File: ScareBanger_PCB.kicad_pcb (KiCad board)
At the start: 2 copper layers, 76 x 56 mm, 17 parts, among them J1 RJ45, J16 Conn_01x10_Female - SAINSMART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, J17 Screw_Terminal_01x10 - HILETG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, J2 1757271, J3 Screw_Terminal_01x06, J4 Barrel_Jack_Switch, J6 Screw_Terminal_01x06, J7 Screw_Terminal_01x06, SW1 SW_SPDT, SW2 SW_SPDT

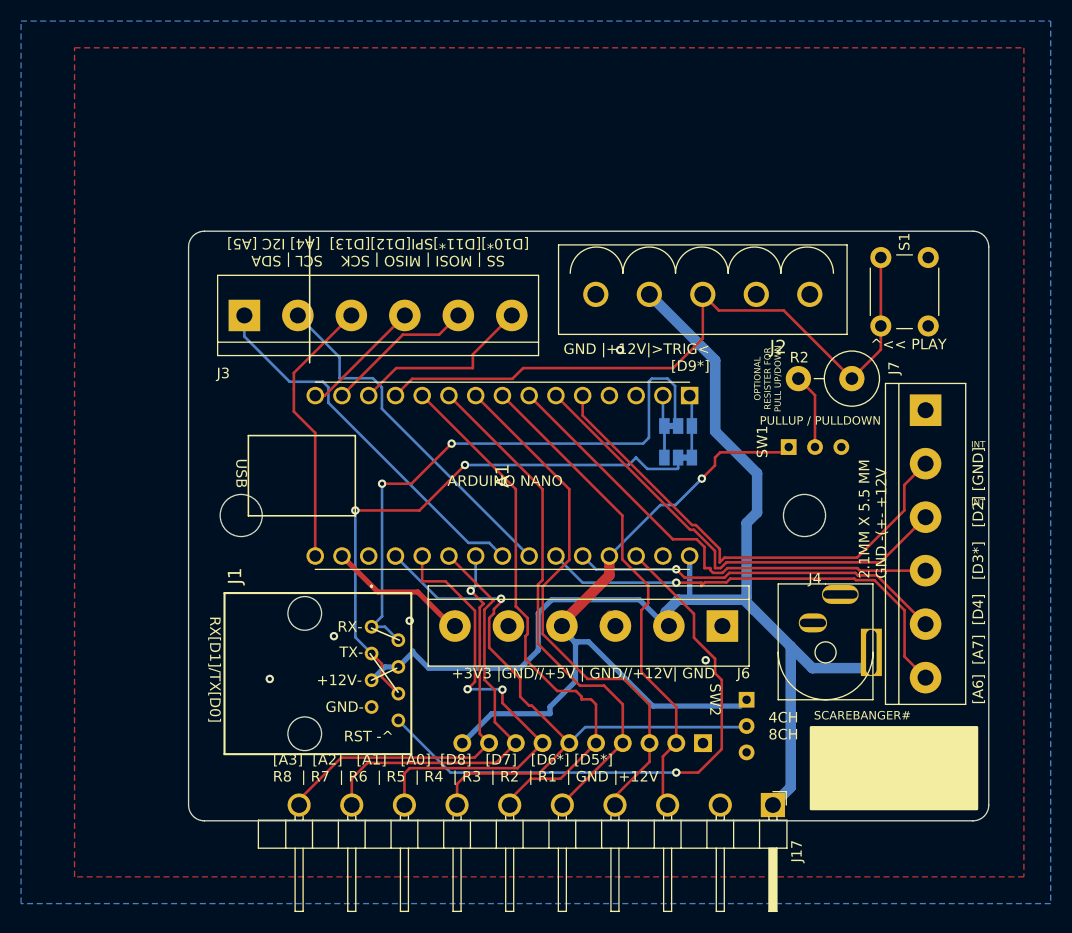
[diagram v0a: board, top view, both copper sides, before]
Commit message: Trigger pin changed to D4
trigger pin switched from D9 to D4 so D9 with its PWM is available for outputs
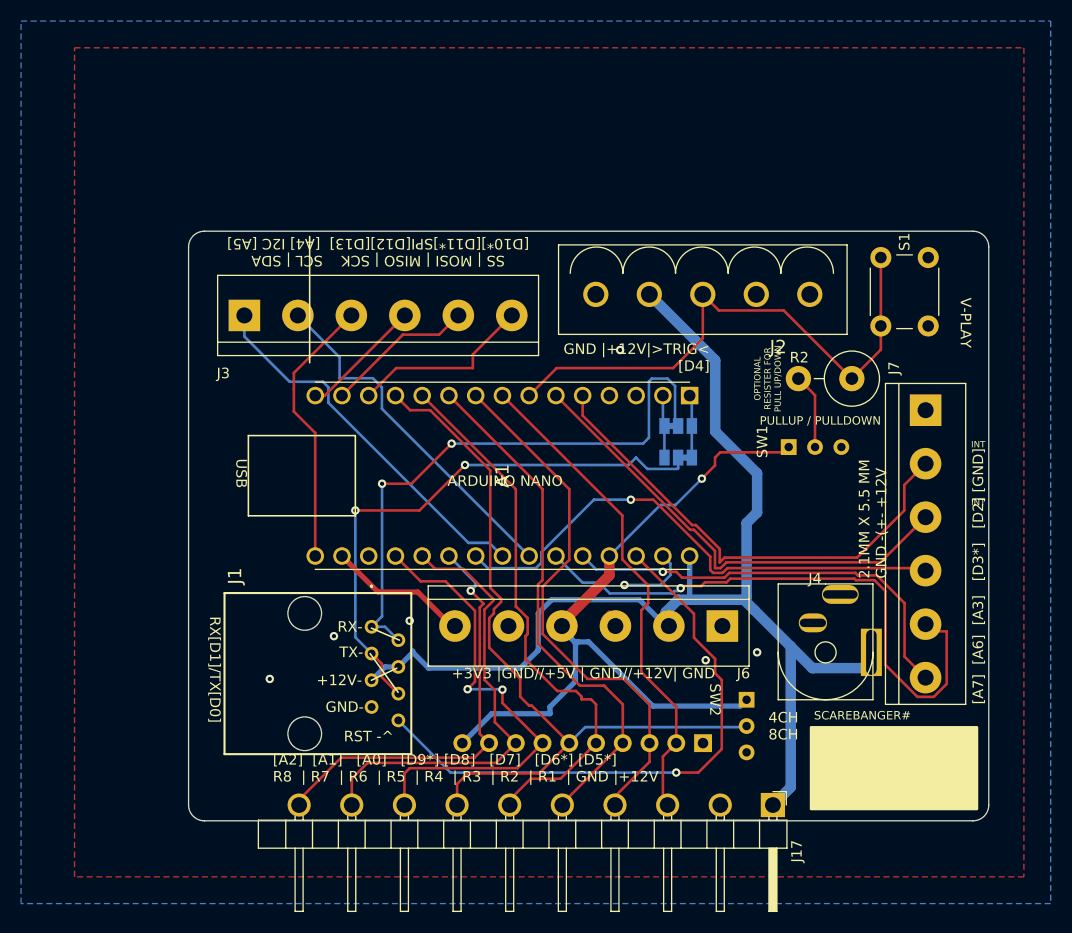
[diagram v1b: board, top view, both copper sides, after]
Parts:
- removed REF** (x2): MountingHole_4mm, MountingHole:MountingHole_4mm
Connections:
- A1 pad 22: Net-(A1-Pad22) -> Net-(J7-Pad4)
- A1 pad 7: Net-(A1-Pad7) -> Net-(J2-Pad3)
- J16 pad 6: Net-(A1-Pad19) -> Net-(A1-Pad12)
- J16 pad 7: Net-(A1-Pad20) -> Net-(A1-Pad19)
- J16 pad 8: Net-(A1-Pad21) -> Net-(A1-Pad20)
- J16 pad 9: Net-(A1-Pad22) -> Net-(A1-Pad21)
- J17 pad 10: Net-(A1-Pad22) -> Net-(A1-Pad21)
- J17 pad 7: Net-(A1-Pad19) -> Net-(A1-Pad12)
- J17 pad 8: Net-(A1-Pad20) -> Net-(A1-Pad19)
- J17 pad 9: Net-(A1-Pad21) -> Net-(A1-Pad20)
- J2 pad 3: Net-(A1-Pad12) -> Net-(J2-Pad3)
- J7 pad 4: Net-(A1-Pad7) -> Net-(J7-Pad4)
- J7 pad 5: Net-(A1-Pad26) -> Net-(A1-Pad25)
- J7 pad 6: Net-(A1-Pad25) -> Net-(A1-Pad26)
- R2 pad 1: Net-(A1-Pad12) -> Net-(J2-Pad3)
- S1 pad 1: Net-(A1-Pad12) -> Net-(J2-Pad3)
- SW2 pad 2: Net-(A1-Pad19) -> Net-(A1-Pad12)
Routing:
- net Net-(J2-Pad3): track 0.00 -> 53.0 mm
- net Net-(J7-Pad4): track 0.00 -> 50.4 mm, vias 0 -> 1
- net Net-(A1-Pad7): track 46.2 -> 0.00 mm
- net Net-(A1-Pad22): track 39.3 -> 0.00 mm, vias 1 -> 0
- net Net-(A1-Pad19): track 60.5 -> 44.2 mm, vias 1 -> 2
- net Net-(A1-Pad25): track 43.2 -> 55.7 mm
- net Net-(A1-Pad12): track 65.7 -> 73.3 mm
- net GND: track 0.72 -> 7.58 mm, vias 5 -> 6
- net Net-(A1-Pad26): track 35.6 -> 40.7 mm
- net Net-(A1-Pad20): track 43.1 -> 42.7 mm, vias 2 -> 0
- net Net-(A1-Pad21): track 40.1 -> 40.3 mm, vias 0 -> 1
- net (no net): vias 0 -> 1
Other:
- board text added: "GND |+12V|>TRIG< [D4]"
- board text added: "V-PLAY"
- board text added: "V2.0"
- board text added: "[A2] [A1] [A0] [D9*] [D8] [D7] [D6*] [D5*] R8 | R7 | R6 | R5 | R4 | R3 | R2 | R1 | GND |+12V"
- board text added: "[A7] [A6] [A3] [D3*] [D2] [GND]"
- board text removed: "GND |+12V|>TRIG< [D9*]"
- board text removed: "V1.2"
- board text removed: "[A3] [A2] [A1] [A0] [D8] [D7] [D6*] [D5*] R8 | R7 | R6 | R5 | R4 | R3 | R2 | R1 | GND |+12V"
- board text removed: "[A6] [A7] [D4] [D3*] [D2] [GND]"
- board text removed: "^<< PLAY"
